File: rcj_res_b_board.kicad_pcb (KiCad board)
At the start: 2 copper layers, 90 x 100 mm, 108 parts, among them P1 GP2Y0A41SK0F, P10 SERVO0, P11 MPU9250, P12 PING0, P13 CONN_01X03, P14 CONN_01X03, P15 CONN_01X04, P16 CONN_01X04, P17 CONN_01X04, P18 CONN_01X04, P19 CONN_01X04, P2 GP2Y0A41SK0F, P3 GP2Y0A41SK0F, P4 GP2Y0A41SK0F, P5 GP2Y0A21YK, P6 GP2Y0A21YK, P7 GP2Y0A21YK, P8 CONN_01X02, P9 CONN_01X02, Q1 Q_PMOS_GSD, SW1 SW_PUSH, SW2 SW_PUSH, SW3 SWITCH_INV, U1 OPB733TR

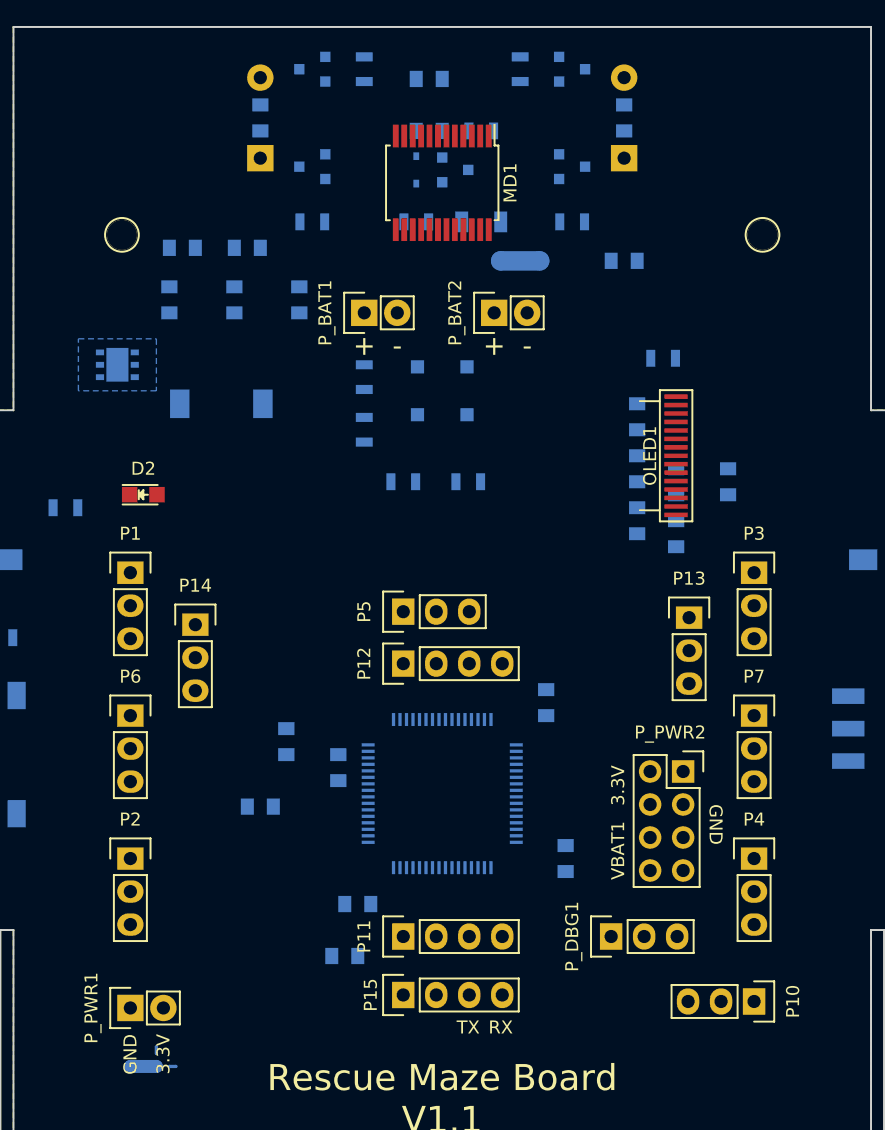
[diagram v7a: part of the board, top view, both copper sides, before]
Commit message: Moved motor driver RCP circuit to front
Rearranged other components to make space
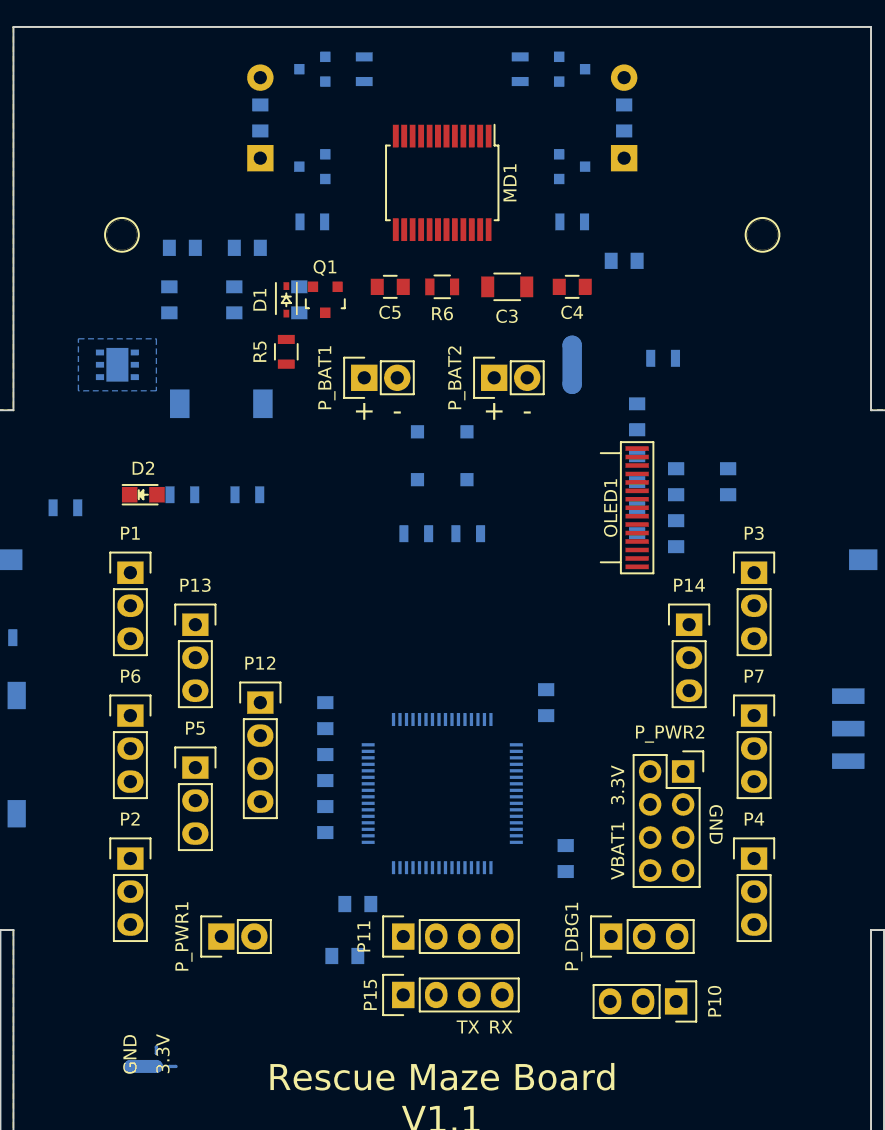
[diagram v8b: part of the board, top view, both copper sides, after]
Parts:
- C3, C4, C5, D1, Q1, R5, R6: moved to F.Cu
- moved P13 38.0 mm to (46.0, 96.0)
- moved P14 38.0 mm to (84.0, 96.0)
- moved P5 20.0 mm to (46.0, 107.0), turned to 270 degrees
- moved R7 17.0 mm to (45.0, 86.0)
- moved R8 17.0 mm to (50.0, 86.0)
- moved C4 16.3 mm to (75.0, 70.0), turned to 0 degrees
- moved C5 16.3 mm to (61.0, 70.0), turned to 0 degrees
- moved R11 14.5 mm to (67.0, 89.0), turned to 0 degrees
- moved D1 14.1 mm to (53.0, 71.0)
- moved Q1 14.1 mm to (56.0, 71.0), turned to 180 degrees
- moved R5 14.1 mm to (53.0, 75.0), turned to 270 degrees
- moved R6 12.4 mm to (65.0, 70.0)
- moved P12 11.4 mm to (51.0, 102.0), turned to 270 degrees
- moved NT1 8.94 mm to (75.0, 76.0), turned to 90 degrees
- moved R9 8.94 mm to (63.0, 89.0), turned to 180 degrees
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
